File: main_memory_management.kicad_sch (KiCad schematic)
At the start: 22 parts, among them U18 27C64

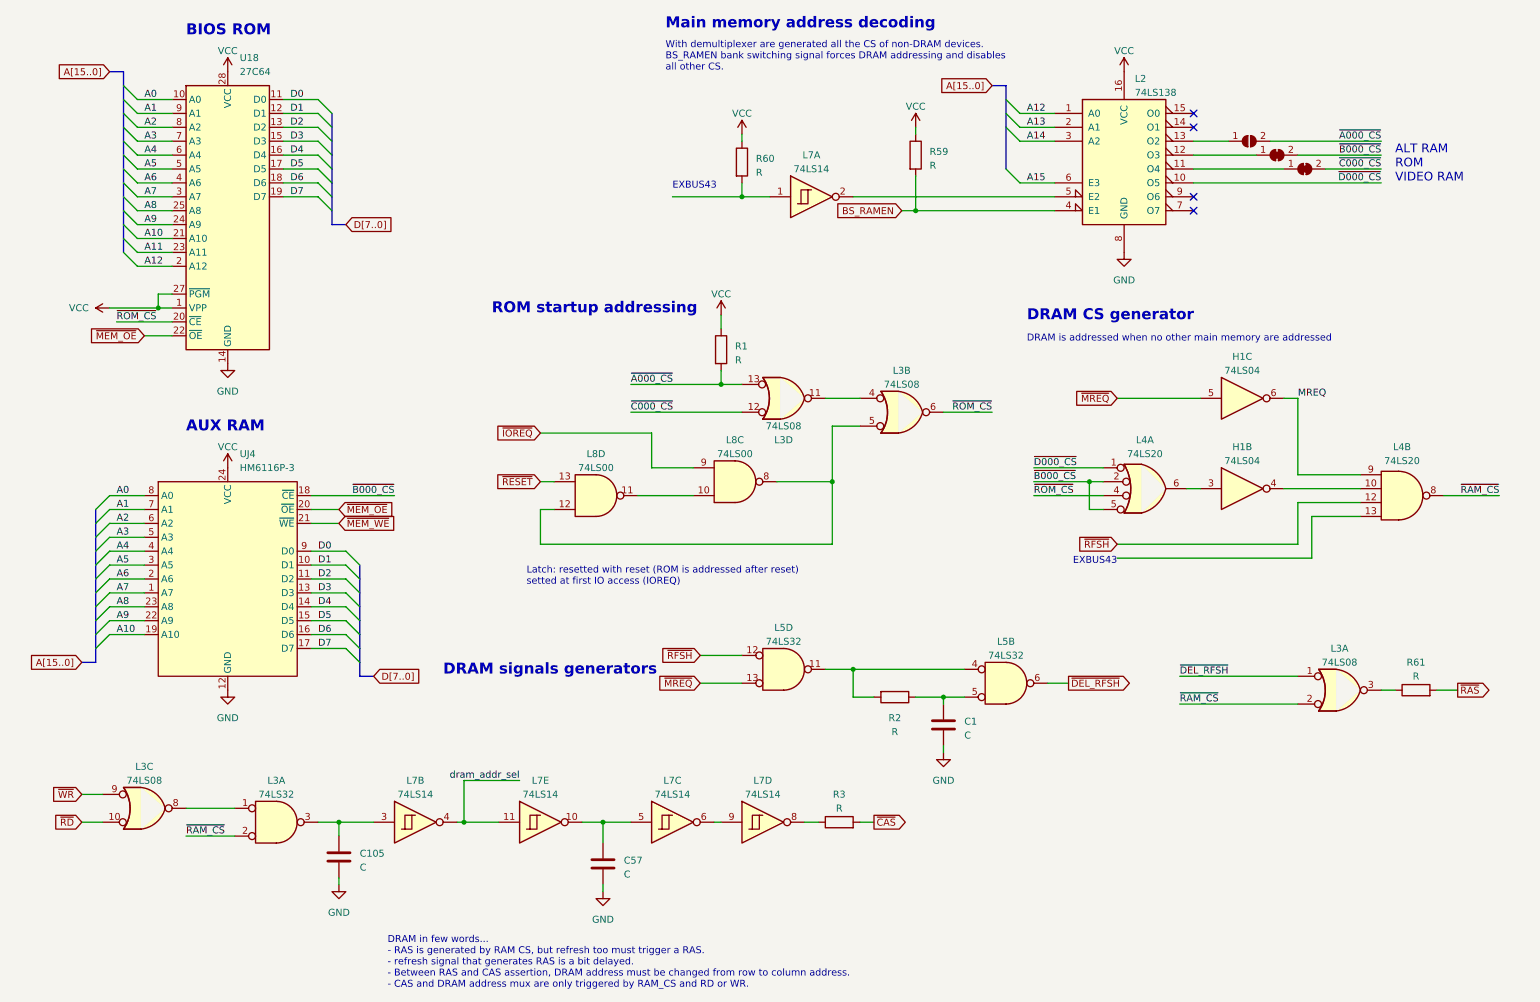
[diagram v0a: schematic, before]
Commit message: Components renaming according to the Uxy convention.
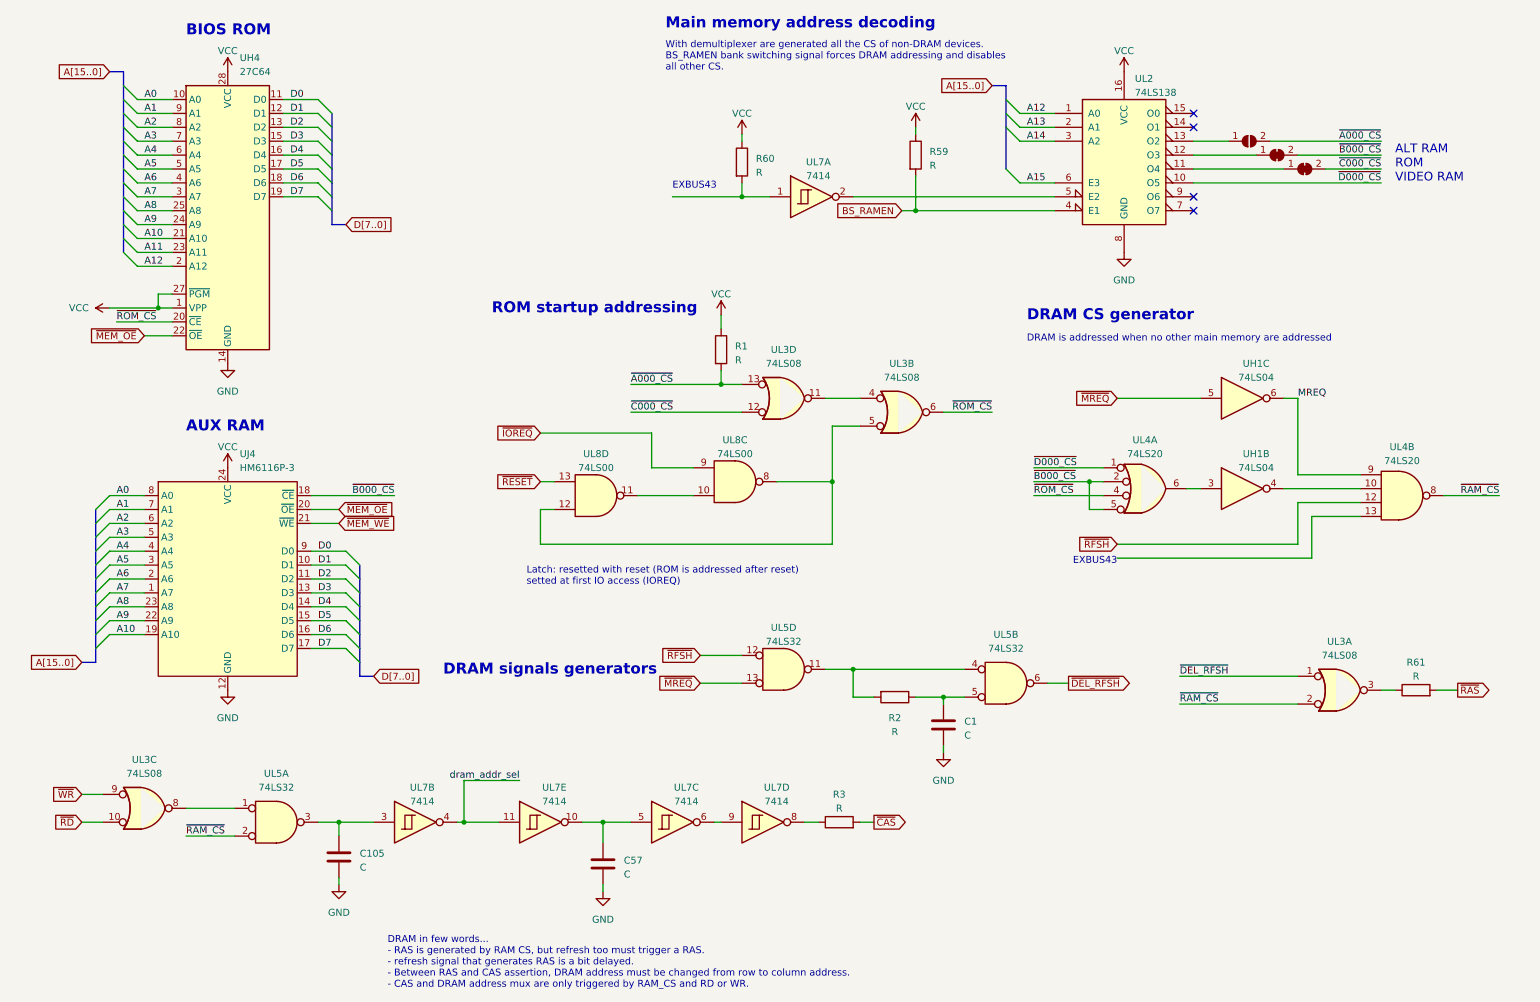
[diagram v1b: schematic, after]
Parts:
- UL7: renamed from L7; value 74LS14 -> 7414
- renumbered H1 to UH1, U18 to UH4, L2 to UL2, L3 to UL3, L4 to UL4, L5 to UL5, L3 to UL5, L8 to UL8

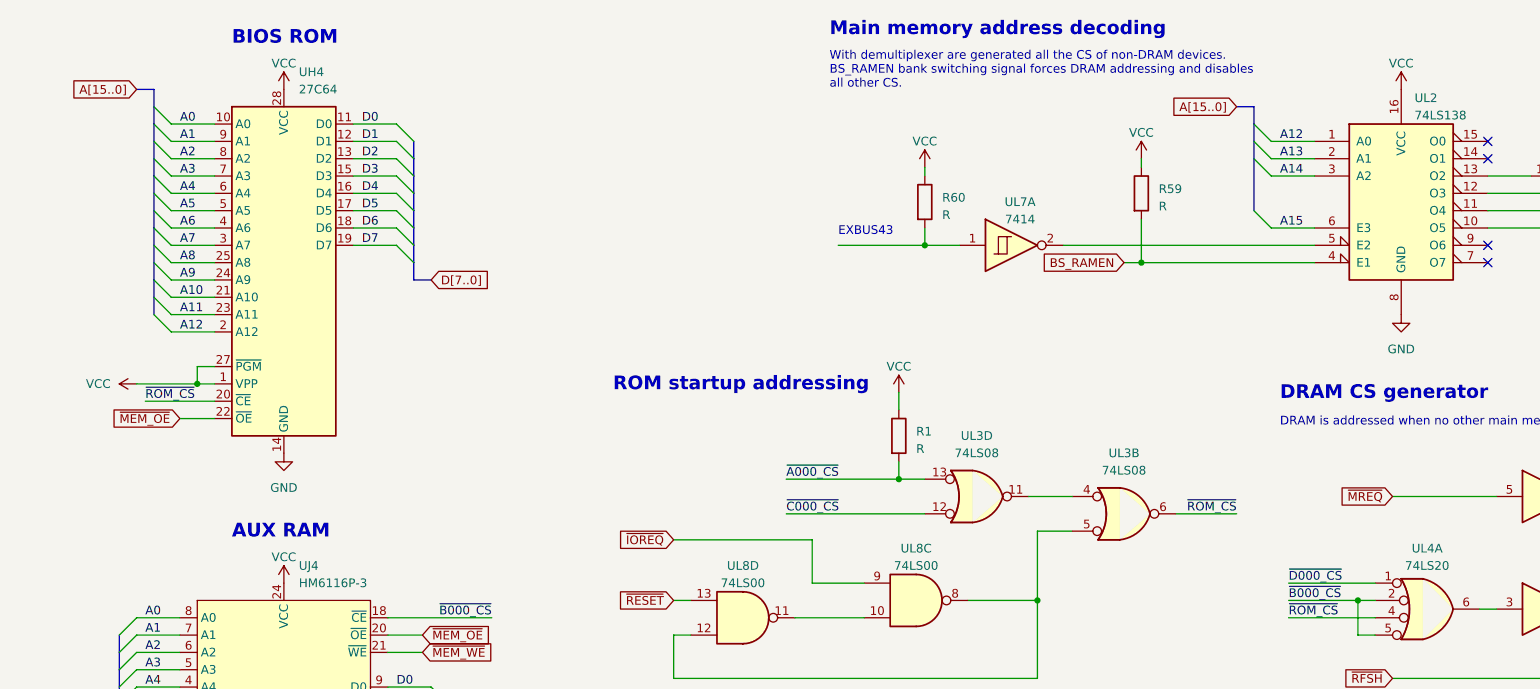
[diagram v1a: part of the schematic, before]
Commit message: VCC -> +5V
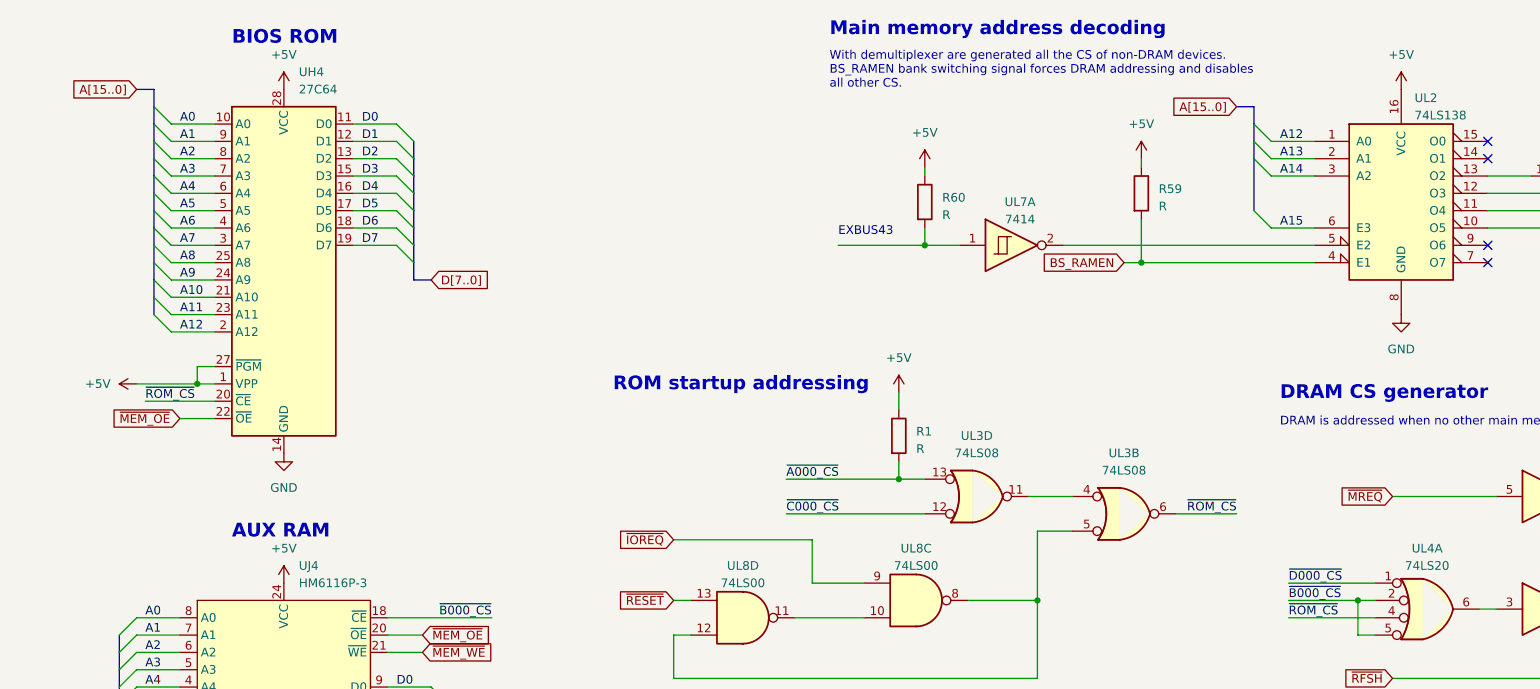
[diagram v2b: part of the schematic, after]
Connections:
- net VCC renamed +5V
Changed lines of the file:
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@@
     )
   )
-  (symbol (lib_id "power:VCC") (at 29.21 68.58 90) (unit 1)
-    (in_bom yes) (on_board yes) (dnp no) (fields_autoplaced)
-    (property "Reference" "#PWR0228" (at 33.02 68.58 0)
-      (effects (font (size 1.27 1.27)) hide)
-    )
-    (property "Value" "VCC" (at 25.4 68.58 90)
+  (symbol (lib_id "power:+5V") (at 29.21 68.58 90) (unit 1)
+    (in_bom yes) (on_board yes) (dnp no) (fields_autoplaced)
+    (property "Reference" "#PWR?" (at 33.02 68.58 0)
+      (effects (font (size 1.27 1.27)) hide)
+    )
+    (property "Value" "+5V" (at 25.4 68.58 90)
       (effects (font (size 1.27 1.27)) (justify left))
     )
@@
       (project "ceda"
         (path "/12a6dbe3-008d-4c5b-88f6-9f1c816060be/4fdb1b90-7ad1-4fa0-9b13-7b81abbda2ba"
-          (reference "#PWR0228") (unit 1)
+          (reference "#PWR?") (unit 1)
         )
       )
@@
     )
   )
-  (symbol (lib_id "power:VCC") (at 176.53 35.56 0) (unit 1)
-    (in_bom yes) (on_board yes) (dnp no) (fields_autoplaced)
-    (property "Reference" "#PWR03" (at 176.53 39.37 0)
-      (effects (font (size 1.27 1.27)) hide)
-    )
-    (property "Value" "VCC" (at 176.53 31.75 0)
+  (symbol (lib_id "power:+5V") (at 176.53 35.56 0) (unit 1)
+    (in_bom yes) (on_board yes) (dnp no) (fields_autoplaced)
+    (property "Reference" "#PWR?" (at 176.53 39.37 0)
+      (effects (font (size 1.27 1.27)) hide)
+    )
+    (property "Value" "+5V" (at 176.53 30.48 0)
       (effects (font (size 1.27 1.27)))
     )
@@
       (project "ceda"
         (path "/12a6dbe3-008d-4c5b-88f6-9f1c816060be/4fdb1b90-7ad1-4fa0-9b13-7b81abbda2ba"
-          (reference "#PWR03") (unit 1)
-        )
-      )
-    )
-  )
-  (symbol (lib_id "power:VCC") (at 140.97 69.85 0) (unit 1)
-    (in_bom yes) (on_board yes) (dnp no) (fields_autoplaced)
-    (property "Reference" "#PWR02" (at 140.97 73.66 0)
-      (effects (font (size 1.27 1.27)) hide)
-    )
-    (property "Value" "VCC" (at 140.97 66.04 0)
+          (reference "#PWR?") (unit 1)
+        )
+      )
+    )
+  )
+  (symbol (lib_id "power:+5V") (at 140.97 69.85 0) (unit 1)
+    (in_bom yes) (on_board yes) (dnp no) (fields_autoplaced)
+    (property "Reference" "#PWR?" (at 140.97 73.66 0)
+      (effects (font (size 1.27 1.27)) hide)
+    )
+    (property "Value" "+5V" (at 140.97 64.77 0)
       (effects (font (size 1.27 1.27)))
     )
@@
       (project "ceda"
         (path "/12a6dbe3-008d-4c5b-88f6-9f1c816060be/4fdb1b90-7ad1-4fa0-9b13-7b81abbda2ba"
-          (reference "#PWR02") (unit 1)
+          (reference "#PWR?") (unit 1)
         )
       )
@@
     )
   )
-  (symbol (lib_id "power:VCC") (at 214.63 25.4 0) (unit 1)
-    (in_bom yes) (on_board yes) (dnp no) (fields_autoplaced)
-    (property "Reference" "#PWR08" (at 214.63 29.21 0)
-      (effects (font (size 1.27 1.27)) hide)
-    )
-    (property "Value" "VCC" (at 214.63 21.59 0)
+  (symbol (lib_id "power:+5V") (at 214.63 25.4 0) (unit 1)
+    (in_bom yes) (on_board yes) (dnp no) (fields_autoplaced)
+    (property "Reference" "#PWR?" (at 214.63 29.21 0)
+      (effects (font (size 1.27 1.27)) hide)
+    )
+    (property "Value" "+5V" (at 214.63 20.32 0)
       (effects (font (size 1.27 1.27)))
     )
@@
       (project "ceda"
         (path "/12a6dbe3-008d-4c5b-88f6-9f1c816060be/4fdb1b90-7ad1-4fa0-9b13-7b81abbda2ba"
-          (reference "#PWR08") (unit 1)
+          (reference "#PWR?") (unit 1)
         )
       )
@@
     )
   )
-  (symbol (lib_id "power:VCC") (at 144.78 36.83 0) (unit 1)
-    (in_bom yes) (on_board yes) (dnp no) (fields_autoplaced)
-    (property "Reference" "#PWR0223" (at 144.78 40.64 0)
-      (effects (font (size 1.27 1.27)) hide)
-    )
-    (property "Value" "VCC" (at 144.78 33.02 0)
+  (symbol (lib_id "power:+5V") (at 144.78 36.83 0) (unit 1)
+    (in_bom yes) (on_board yes) (dnp no) (fields_autoplaced)
+    (property "Reference" "#PWR?" (at 144.78 40.64 0)
+      (effects (font (size 1.27 1.27)) hide)
+    )
+    (property "Value" "+5V" (at 144.78 31.75 0)
       (effects (font (size 1.27 1.27)))
     )
@@
       (project "ceda"
         (path "/12a6dbe3-008d-4c5b-88f6-9f1c816060be/4fdb1b90-7ad1-4fa0-9b13-7b81abbda2ba"
-          (reference "#PWR0223") (unit 1)
+          (reference "#PWR?") (unit 1)
         )
       )
@@
     )
   )
-  (symbol (lib_id "power:VCC") (at 50.8 97.79 0) (unit 1)
-    (in_bom yes) (on_board yes) (dnp no) (fields_autoplaced)
-    (property "Reference" "#PWR0225" (at 50.8 101.6 0)
-      (effects (font (size 1.27 1.27)) hide)
-    )
-    (property "Value" "VCC" (at 50.8 93.98 0)
+  (symbol (lib_id "power:+5V") (at 50.8 97.79 0) (unit 1)
+    (in_bom yes) (on_board yes) (dnp no) (fields_autoplaced)
+    (property "Reference" "#PWR?" (at 50.8 101.6 0)
+      (effects (font (size 1.27 1.27)) hide)
+    )
+    (property "Value" "+5V" (at 50.8 92.71 0)
       (effects (font (size 1.27 1.27)))
     )
@@
       (project "ceda"
         (path "/12a6dbe3-008d-4c5b-88f6-9f1c816060be/4fdb1b90-7ad1-4fa0-9b13-7b81abbda2ba"
-          (reference "#PWR0225") (unit 1)
+          (reference "#PWR?") (unit 1)
         )
       )
@@
     )
   )
-  (symbol (lib_id "power:VCC") (at 50.8 25.4 0) (unit 1)
-    (in_bom yes) (on_board yes) (dnp no) (fields_autoplaced)
-    (property "Reference" "#PWR0224" (at 50.8 29.21 0)
-      (effects (font (size 1.27 1.27)) hide)
-    )
-    (property "Value" "VCC" (at 50.8 21.59 0)
+  (symbol (lib_id "power:+5V") (at 50.8 25.4 0) (unit 1)
+    (in_bom yes) (on_board yes) (dnp no) (fields_autoplaced)
+    (property "Reference" "#PWR?" (at 50.8 29.21 0)
+      (effects (font (size 1.27 1.27)) hide)
+    )
+    (property "Value" "+5V" (at 50.8 20.32 0)
       (effects (font (size 1.27 1.27)))
     )
@@
       (project "ceda"
         (path "/12a6dbe3-008d-4c5b-88f6-9f1c816060be/4fdb1b90-7ad1-4fa0-9b13-7b81abbda2ba"
-          (reference "#PWR0224") (unit 1)
-        )
-      )
+          (reference "#PWR?") (unit 1)
+        )
+      )

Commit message: Notes in kicad's sheet text blocks
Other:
- company: (none) -> Logic Systems Int'l Inc
- title: (none) -> CEDA - Sanco 8003 schematics
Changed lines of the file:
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@@
 (kicad_sch (version 20230121) (generator eeschema)
   (paper "A4")
+  (title_block
+    (title "CEDA - Sanco 8003 schematics")
+    (rev "05")
+    (company "Logic Systems Int'l Inc")
+    (comment 1 "reversed by RetrOfficina - retrofficina.glgprograms.it")
+    (comment 2 "do some startup tricks with ROM")
+    (comment 3 "Decode the access to the main Z80 addressing space, plus handle DRAM refresh and")
+    (comment 4 "Main Memory Management")
+  )
   (junction (at 144.78 48.26) (diameter 0) (color 0 0 0 0)
   )
